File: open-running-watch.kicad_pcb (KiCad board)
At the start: 4 copper layers, 41 x 61.9 mm, 207 parts, among them IC1 BLUENRG-232N, IC10 NXB0108BQX, IC11 STM32L475RGT6, IC12 W25N512GVEIG, IC13 TPS613222ADBVR, IC14 INA186A5IYFDR, IC15 INA186A5IYFDR, IC16 INA186A5IYFDR, IC17 INA186A5IYFDR, IC18 PCAL9538ABSHP, IC19 INA186A5IYFDR, IC2 TESEO-LIV3F, IC20 INA186A5IYFDR, IC21 LSF0204GU12X, IC22 INA186A5IYFDR, IC3 BGA_725L6_E6327, IC4 BQ27441DRZR-G1A, IC5 MCP73811T-420I_OT, IC6 TPS62237DRYR, IC7 ST1S15J18R, IC8 TLV9002SIRUGR, IC9 ICP-10100, J1 20021121-00014T4LF, J2 10118192-0001LF, J3 1-2328702-0, J4 2328702-4, Q1 BC847BS, Q2 BC847BS, Q3 BC817-25-QVL, Q4 BC847, T1 BALF-NRG-02D3, U1 TPS62233DRYR, Y1 ECS-320-12-37B2-7KM-TR, Y2 NX3215SA-32.768K-EXS00A-MU000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, Y3 ECS-.327-7-1210-TR

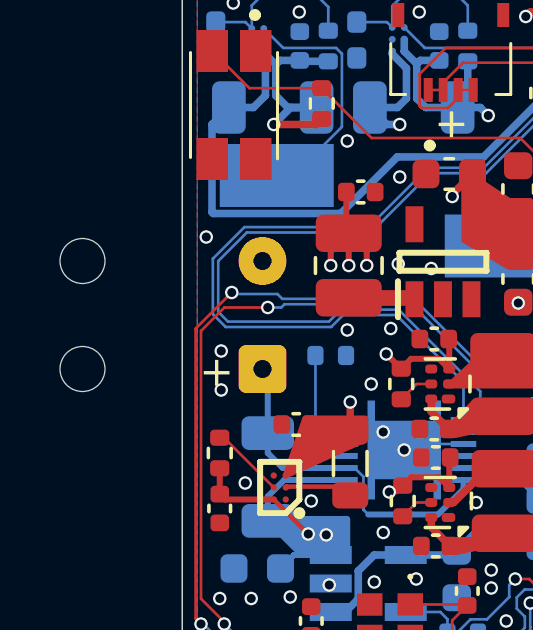
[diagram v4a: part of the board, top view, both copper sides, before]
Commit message: Changed battery connection footprint
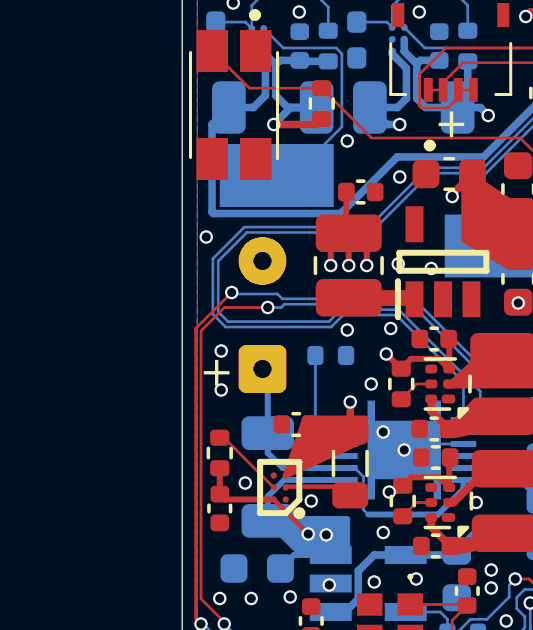
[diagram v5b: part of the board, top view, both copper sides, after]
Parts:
- BT1: footprint Connector_Wire:SolderWire-0.1sqmm_1x02_P3.6mm_D0.4mm_OD1mm_Relief -> Connector_Wire:SolderWire-0.1sqmm_1x02_P3.6mm_D0.4mm_OD1mm
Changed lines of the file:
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@@
 			(at 0 0 180)
 			(layer "B.SilkS")
-			(hide yes)
 			(effects
 				(font
@@
 		)
 	)
-	(footprint "Connector_Wire:SolderWire-0.1sqmm_1x02_P3.6mm_D0.4mm_OD1mm_Relief"
+	(footprint "Connector_Wire:SolderWire-0.1sqmm_1x02_P3.6mm_D0.4mm_OD1mm"
 		(layer "B.Cu")
 		(at 132.175 86.9 90)
-		(descr "Soldered wire connection with feed through strain relief, for 2 times 0.1 mm² wires, basic insulation, conductor diameter 0.4mm, outer diameter 1mm, size source Multi-Contact FLEXI-E 0.1 (https://ec.staubli.com/AcroFiles/Catalogues/TM_Cab-Main-11014119_(en)_hi.pdf), bend radius 3 times outer diameter, generated with kicad-footprint-generator")
-		(tags "connector wire 0.1sqmm strain-relief")
+		(descr "Soldered wire connection, for 2 times 0.1 mm² wires, basic insulation, conductor diameter 0.4mm, outer diameter 1mm, size source Multi-Contact FLEXI-E 0.1 (https://ec.staubli.com/AcroFiles/Catalogues/TM_Cab-Main-11014119_(en)_hi.pdf), bend radius 3 times outer diameter, generated with kicad-footprint-generator")
+		(tags "connector wire 0.1sqmm")
 		(property "Reference" "BT1"
-			(at 1.8 2 -90)
+			(at 1.8 2 90)
 			(layer "B.SilkS")
-			(hide yes)
 			(effects
 				(font
@@
 		)
 		(property "Value" "Battery"
-			(at 1.8 -7.95 -90)
+			(at 1.8 -2 90)
 			(layer "B.Fab")
 			(effects
@@
 			)
 		)
-		(property "Footprint" "Connector_Wire:SolderWire-0.1sqmm_1x02_P3.6mm_D0.4mm_OD1mm_Relief"
+		(property "Footprint" "Connector_Wire:SolderWire-0.1sqmm_1x02_P3.6mm_D0.4mm_OD1mm"
 			(at 0 0 -90)
 			(unlocked yes)
@@
 		(attr exclude_from_pos_files exclude_from_bom)
 		(fp_line
-			(start 4.21 -5.39)
-			(end 4.21 -1.06)
-			(stroke
-				(width 0.12)
-				(type solid)
-			)
-			(layer "B.SilkS")
-		)
-		(fp_line
-			(start 2.99 -5.39)
-			(end 2.99 -1.06)
-			(stroke
-				(width 0.12)
-				(type solid)
-			)
-			(layer "B.SilkS")
-		)
-		(fp_line
-			(start 0.61 -5.39)
-			(end 0.61 -1.06)
-			(stroke
-				(width 0.12)
-				(type solid)
-			)
-			(layer "B.SilkS")
-		)
-		(fp_line
-			(start -0.61 -5.39)
-			(end -0.61 -1.06)
-			(stroke
-				(width 0.12)
-				(type solid)
-			)
-			(layer "B.SilkS")
-		)
-		(fp_line
-			(start 4.9 -7.25)
-			(end 2.3 -7.25)
+			(start 4.9 -1.3)
+			(end 2.3 -1.3)
 			(stroke
 				(width 0.05)
@@
 		)
 		(fp_line
-			(start 2.3 -7.25)
+			(start 2.3 -1.3)
 			(end 2.3 1.3)
 			(stroke
@@
 		)
 		(fp_line
-			(start 1.3 -7.25)
-			(end -1.3 -7.25)
+			(start 1.3 -1.3)
+			(end -1.3 -1.3)
 			(stroke
 				(width 0.05)
@@
 		)
 		(fp_line
-			(start -1.3 -7.25)
+			(start -1.3 -1.3)
 			(end -1.3 1.3)
 			(stroke
@@
 		(fp_line
 			(start 4.9 1.3)
-			(end 4.9 -7.25)
+			(end 4.9 -1.3)
 			(stroke
 				(width 0.05)
@@
 		(fp_line
 			(start 1.3 1.3)
-			(end 1.3 -7.25)
+			(end 1.3 -1.3)
 			(stroke
 				(width 0.05)
@@
 			(layer "B.CrtYd")
 		)
-		(fp_line
-			(start 4.9 -7.25)
-			(end 2.3 -7.25)
-			(stroke
-				(width 0.05)
-				(type solid)
-			)
-			(layer "F.CrtYd")
-		)
-		(fp_line
-			(start 2.3 -7.25)
-			(end 2.3 -4.75)
-			(stroke
-				(width 0.05)
-				(type solid)
-			)
-			(layer "F.CrtYd")
-		)
-		(fp_line
-			(start 1.3 -7.25)
-			(end -1.3 -7.25)
-			(stroke
-				(width 0.05)
-				(type solid)
-			)
-			(layer "F.CrtYd")
-		)
-		(fp_line
-			(start -1.3 -7.25)
-			(end -1.3 -4.75)
-			(stroke
-				(width 0.05)
-				(type solid)
-			)
-			(layer "F.CrtYd")
-		)
-		(fp_line
-			(start 4.9 -4.75)
-			(end 4.9 -7.25)
-			(stroke
-				(width 0.05)
-				(type solid)
-			)
-			(layer "F.CrtYd")
-		)
-		(fp_line
-			(start 2.3 -4.75)
-			(end 4.9 -4.75)
-			(stroke
-				(width 0.05)
-				(type solid)
-			)
-			(layer "F.CrtYd")
-		)
-		(fp_line
-			(start 1.3 -4.75)
-			(end 1.3 -7.25)
-			(stroke
-				(width 0.05)
-				(type solid)
-			)
-			(layer "F.CrtYd")
-		)
-		(fp_line
-			(start -1.3 -4.75)
-			(end 1.3 -4.75)
-			(stroke
-				(width 0.05)
-				(type solid)
-			)
-			(layer "F.CrtYd")
-		)
-		(fp_line
-			(start 4.1 -6)
-			(end 4.1 0)
-			(stroke
-				(width 0.1)
-				(type solid)
-			)
-			(layer "B.Fab")
-		)
-		(fp_line
-			(start 3.1 -6)
-			(end 3.1 0)
-			(stroke
-				(width 0.1)
-				(type solid)
-			)
-			(layer "B.Fab")
-		)
-		(fp_line
-			(start 0.5 -6)
-			(end 0.5 0)
-			(stroke
-				(width 0.1)
-				(type solid)
-			)
-			(layer "B.Fab")
-		)
-		(fp_line
-			(start -0.5 -6)
-			(end -0.5 0)
-			(stroke
-				(width 0.1)
-				(type solid)
-			)
-			(layer "B.Fab")
-		)
-		(fp_circle
-			(center 3.6 -6)
-			(end 4.1 -6)
-			(stroke
-				(width 0.1)
-				(type solid)
-			)
-			(fill none)
-			(layer "B.Fab")
-		)
-		(fp_circle
-			(center 0 -6)
-			(end 0.5 -6)
-			(stroke
-				(width 0.1)
-				(type solid)
-			)
-			(fill none)
-			(layer "B.Fab")
-		)
 		(fp_circle
 			(center 3.6 0)
@@
 		)
 		(fp_text user "${REFERENCE}"
-			(at 1.8 -3 0)
+			(at 1.8 0 180)
 			(layer "B.Fab")
 			(effects
 				(font
-					(size 0.8 0.8)
-					(thickness 0.12)
+					(size 0.65 0.65)
+					(thickness 0.1)
 				)
 				(justify mirror)
 			)
 		)
-		(pad "" np_thru_hole circle
-			(at 0 -6 90)
-			(size 1.5 1.5)
-			(drill 1.5)
-			(layers "*.Cu" "*.Mask")
-		)
-		(pad "" np_thru_hole circle
-			(at 3.6 -6 90)
-			(size 1.5 1.5)
-			(drill 1.5)
-			(layers "*.Cu" "*.Mask")
-		)
 		(pad "1" thru_hole roundrect
 			(at 0 0 90)
@@
 			(pintype "passive")
 		)
-		(model "${KICAD8_3DMODEL_DIR}/Connector_Wire.3dshapes/SolderWire-0.1sqmm_1x02_P3.6mm_D0.4mm_OD1mm_Relief.wrl"
+		(model "${KICAD8_3DMODEL_DIR}/Connector_Wire.3dshapes/SolderWire-0.1sqmm_1x02_P3.6mm_D0.4mm_OD1mm.wrl"
 			(offset
 				(xyz 0 0 0)

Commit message: Added 'sponsored by PCBWay' silkscreen
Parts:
- added G***: LOGO, pcbway-logo:pcbway-logo, B.Cu at (150.1, 91.8)
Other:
- board text added: "Sponsored by"
